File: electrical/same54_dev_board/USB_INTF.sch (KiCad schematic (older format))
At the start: 3 parts, among them J1 USB_B_Micro, U2 FT232RQ-REEL

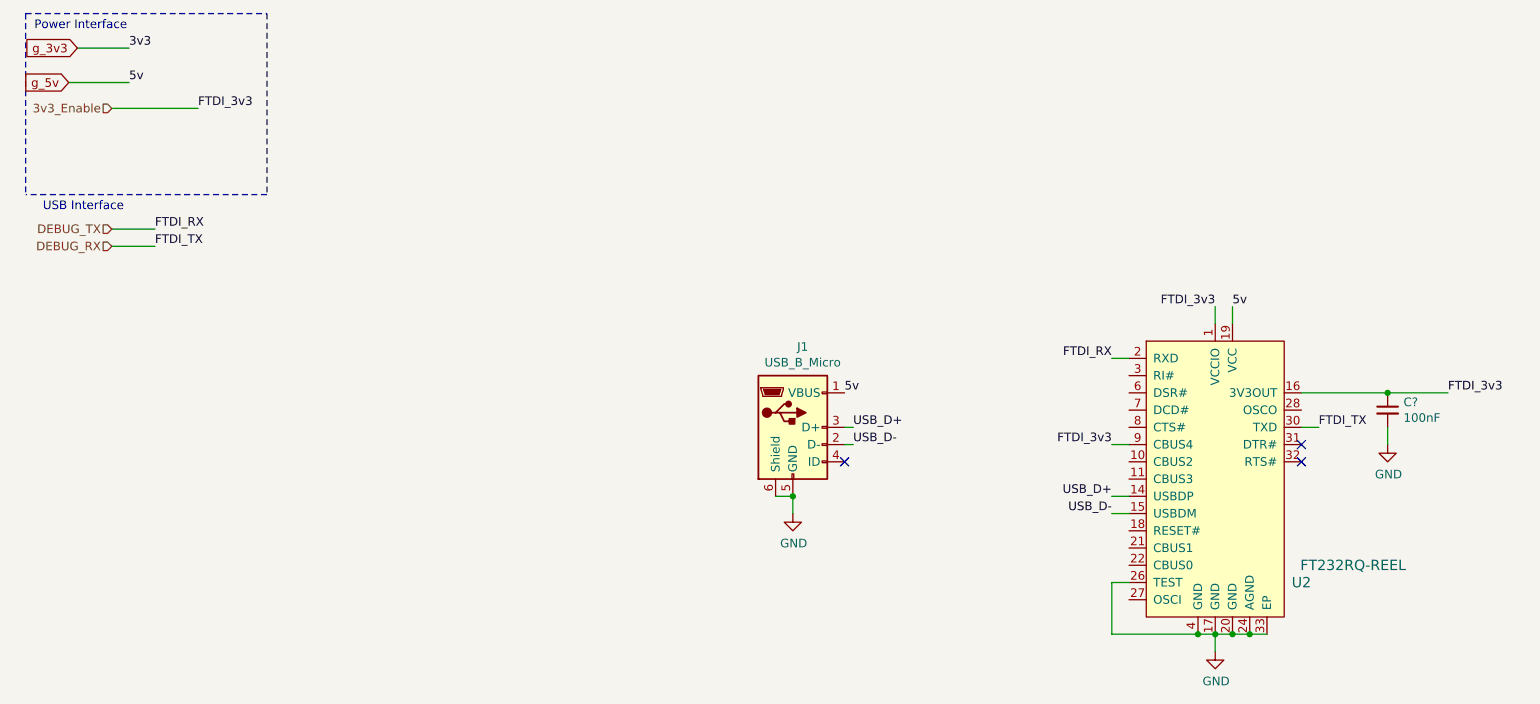
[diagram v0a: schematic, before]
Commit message: going with barrel jack 5v+2A optional input, with usb supplying 400mA + 100mA for internals
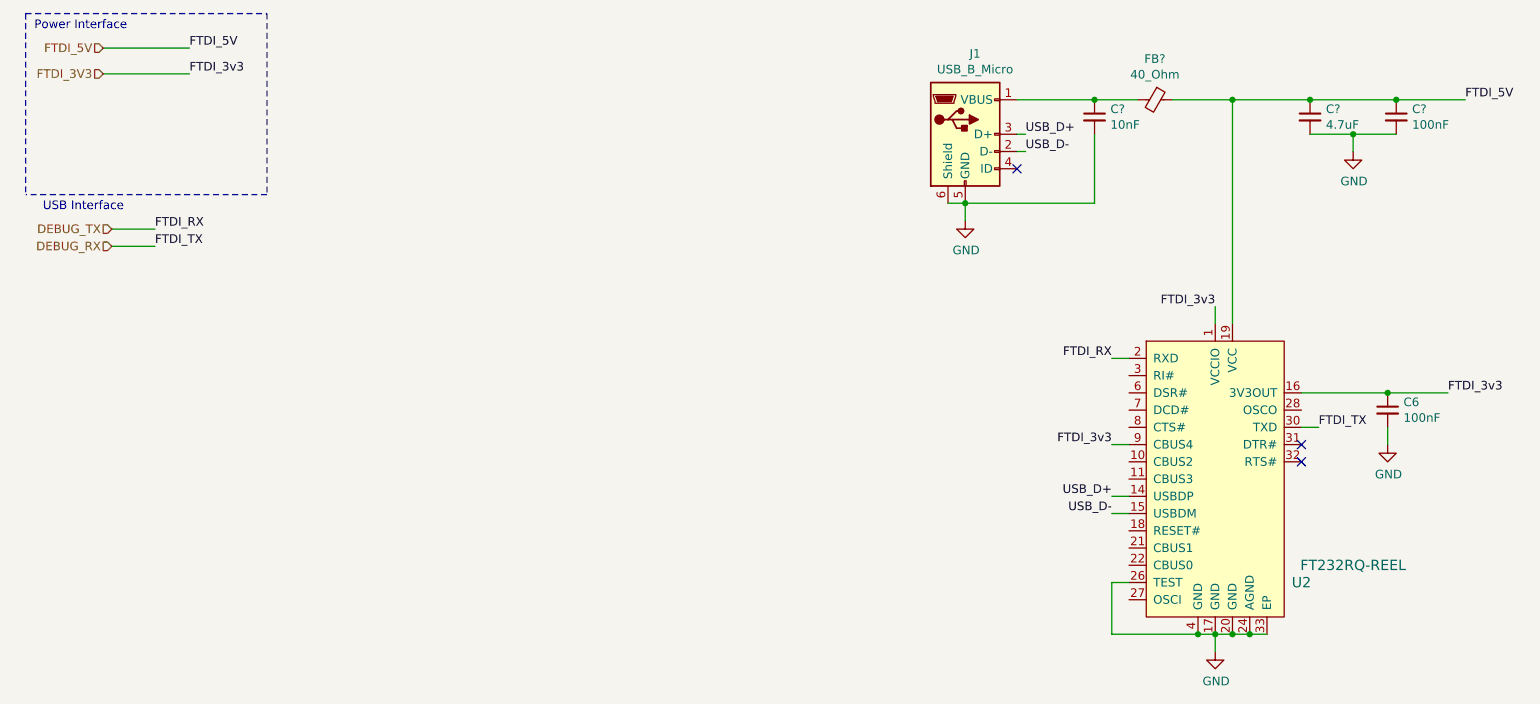
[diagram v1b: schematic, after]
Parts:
- added C?: 10nF, symbol Device:C_Small
- added C?: 4.7uF, symbol Device:C_Small
- added C?: 100nF, symbol Device:C_Small
- added FB?: 40_Ohm, symbol Device:Ferrite_Bead_Small
- gave numbers to parts that had none: 1
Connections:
- net GND: now also C?.2, C?.2, C?.2
- net 3v3_Enable renamed FTDI_3V3
- net g_5v: no longer names the net of J1.1 (VBUS)
- net g_5v: now also C?.1, FB?.2; no longer U2.19 (VCC)
- new net FTDI_5V: C?.1, C?.1, FB?.1, U2.19 (VCC)
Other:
- moved on the sheet: J1
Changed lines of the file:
@@
 Comment4 ""
 $EndDescr
-Text GLabel 900  800  0    50   Input ~ 0
-g_3v3
-Text GLabel 850  1000 0    50   Input ~ 0
-g_5v
-Wire Wire Line
-	900  800  1200 800
-Text Label 1200 800  0    50   ~ 0
-3v3
-Wire Wire Line
-	850  1000 1200 1000
-Text Label 1200 1000 0    50   ~ 0
-5v
 $Comp
 L Connector:USB_B_Micro J1
 U 1 1 5E8480AD
-P 5050 3000
-F 0 "J1" H 5107 3467 50  0000 C CNN
-F 1 "USB_B_Micro" H 5107 3376 50  0000 C CNN
-F 2 "Connector_USB:USB_Micro-B_Wuerth_629105150521" H 5200 2950 50  0001 C CNN
-F 3 "~" H 5200 2950 50  0001 C CNN
-	1    5050 3000
+P 6050 1300
+F 0 "J1" H 6107 1767 50  0000 C CNN
+F 1 "USB_B_Micro" H 6107 1676 50  0000 C CNN
+F 2 "Connector_USB:USB_Micro-B_Wuerth_629105150521" H 6200 1250 50  0001 C CNN
+F 3 "~" H 6200 1250 50  0001 C CNN
+	1    6050 1300
 	1    0    0    -1
 $EndComp
@@
 Power Interface
 Wire Wire Line
-	5350 3000 5400 3000
-Text Label 5400 3000 0    50   ~ 0
+	6350 1300 6400 1300
+Text Label 6400 1300 0    50   ~ 0
 USB_D+
 Wire Wire Line
-	5350 3100 5400 3100
-Text Label 5400 3100 0    50   ~ 0
+	6350 1400 6400 1400
+Text Label 6400 1400 0    50   ~ 0
 USB_D-
 Wire Wire Line
@@
 	7500 4200 7500 4300
 $Comp
-L power:GND #PWR?
+L power:GND #PWR0110
 U 1 1 5E7B73F2
 P 7500 4300
-F 0 "#PWR?" H 7500 4050 50  0001 C CNN
+F 0 "#PWR0110" H 7500 4050 50  0001 C CNN
 F 1 "GND" H 7505 4127 50  0000 C CNN
 F 2 "" H 7500 4300 50  0001 C CNN
@@
 $EndComp
 Wire Wire Line
-	4950 3400 5050 3400
-Wire Wire Line
-	5050 3400 5050 3500
-Connection ~ 5050 3400
-$Comp
-L power:GND #PWR?
+	5950 1700 6050 1700
+Wire Wire Line
+	6050 1700 6050 1800
+Connection ~ 6050 1700
+$Comp
+L power:GND #PWR0111
 U 1 1 5E7BED3A
-P 5050 3500
-F 0 "#PWR?" H 5050 3250 50  0001 C CNN
-F 1 "GND" H 5055 3327 50  0000 C CNN
-F 2 "" H 5050 3500 50  0001 C CNN
-F 3 "" H 5050 3500 50  0001 C CNN
-	1    5050 3500
-	1    0    0    -1
-$EndComp
-Text Label 5350 2800 0    50   ~ 0
-5v
-NoConn ~ 5350 3200
+P 6050 1800
+F 0 "#PWR0111" H 6050 1550 50  0001 C CNN
+F 1 "GND" H 6055 1627 50  0000 C CNN
+F 2 "" H 6050 1800 50  0001 C CNN
+F 3 "" H 6050 1800 50  0001 C CNN
+	1    6050 1800
+	1    0    0    -1
+$EndComp
+NoConn ~ 6350 1500
 Wire Notes Line
 	600  600  2000 600
-Wire Wire Line
-	7600 2400 7600 2300
-Text Label 7600 2300 0    50   ~ 0
-5v
 Text Label 1350 1950 0    50   ~ 0
 FTDI_TX
@@
 Text Notes 700  1750 0    50   ~ 0
 USB Interface
-Text HLabel 1100 1150 0    50   Input ~ 0
-3v3_Enable
 Wire Notes Line
 	2000 1650 600  1650
 Wire Notes Line
-	2000 600  2000 1650
-Wire Notes Line
 	600  600  600  1650
 Wire Wire Line
 	7500 2300 7500 2400
 Wire Wire Line
-	1100 1150 1600 1150
-Text Label 1600 1150 0    50   ~ 0
-FTDI_3v3
-Wire Wire Line
 	8000 2800 8500 2800
 $Comp
-L Device:C_Small C?
+L Device:C_Small C6
 U 1 1 5E7E8395
 P 8500 2900
-F 0 "C?" H 8592 2946 50  0000 L CNN
+F 0 "C6" H 8592 2946 50  0000 L CNN
 F 1 "100nF" H 8592 2855 50  0000 L CNN
 F 2 "" H 8500 2900 50  0001 C CNN
@@
 	8500 3000 8500 3100
 $Comp
-L power:GND #PWR?
+L power:GND #PWR0112
 U 1 1 5E7E91F3
 P 8500 3100
-F 0 "#PWR?" H 8500 2850 50  0001 C CNN
+F 0 "#PWR0112" H 8500 2850 50  0001 C CNN
 F 1 "GND" H 8505 2927 50  0000 C CNN
 F 2 "" H 8500 3100 50  0001 C CNN
@@
 	7700 4200 7800 4200
 Connection ~ 7700 4200
+$Comp
+L Device:C_Small C?
+U 1 1 5E7F85B7
+P 6800 1200
+F 0 "C?" H 6892 1246 50  0000 L CNN
+F 1 "10nF" H 6892 1155 50  0000 L CNN
+F 2 "" H 6800 1200 50  0001 C CNN
+F 3 "~" H 6800 1200 50  0001 C CNN
+	1    6800 1200
+	1    0    0    -1
+$EndComp
+Wire Wire Line
+	6350 1100 6800 1100
+Wire Wire Line
+	6800 1300 6800 1700
+Wire Wire Line
+	6800 1700 6050 1700
+Wire Wire Line
+	6800 1100 7050 1100
+Connection ~ 6800 1100
+$Comp
+L Device:Ferrite_Bead_Small FB?
+U 1 1 5E7FB1E4
+P 7150 1100
+F 0 "FB?" V 6913 1100 50  0000 C CNN
+F 1 "40_Ohm" V 7004 1100 50  0000 C CNN
+F 2 "" V 7080 1100 50  0001 C CNN
+F 3 "~" H 7150 1100 50  0001 C CNN
+	1    7150 1100
+	0    1    1    0
+$EndComp
+Wire Wire Line
+	7600 1100 7600 2400
+Wire Wire Line
+	7250 1100 7600 1100
+Wire Wire Line
+	7600 1100 8050 1100
+Connection ~ 7600 1100
+$Comp
+L Device:C_Small C?
+U 1 1 5E8424CD
+P 8050 1200
+F 0 "C?" H 8142 1246 50  0000 L CNN
+F 1 "4.7uF" H 8142 1155 50  0000 L CNN
+F 2 "" H 8050 1200 50  0001 C CNN
+F 3 "~" H 8050 1200 50  0001 C CNN
+	1    8050 1200
+	1    0    0    -1
+$EndComp
+$Comp
+L Device:C_Small C?
+U 1 1 5E844B56
+P 8550 1200
+F 0 "C?" H 8642 1246 50  0000 L CNN
+F 1 "100nF" H 8642 1155 50  0000 L CNN
+F 2 "" H 8550 1200 50  0001 C CNN
+F 3 "~" H 8550 1200 50  0001 C CNN
+	1    8550 1200
+	1    0    0    -1
+$EndComp
+Wire Wire Line
+	8050 1100 8550 1100
+Connection ~ 8050 1100
+Wire Wire Line
+	8050 1300 8300 1300
+Wire Wire Line
+	8300 1300 8300 1400
+Connection ~ 8300 1300
+Wire Wire Line
+	8300 1300 8550 1300
+$Comp
+L power:GND #PWR?
+U 1 1 5E849ABD
+P 8300 1400
+F 0 "#PWR?" H 8300 1150 50  0001 C CNN
+F 1 "GND" H 8305 1227 50  0000 C CNN
+F 2 "" H 8300 1400 50  0001 C CNN
+F 3 "" H 8300 1400 50  0001 C CNN
+	1    8300 1400
+	1    0    0    -1
+$EndComp
+Text Label 8950 1100 0    50   ~ 0
+FTDI_5V
+Wire Wire Line
+	8550 1100 8950 1100
+Connection ~ 8550 1100
+Wire Wire Line
+	1050 800  1550 800
+Text Label 1550 800  0    50   ~ 0
+FTDI_5V
+Text HLabel 1050 800  0    50   Input ~ 0
+FTDI_5V
+Text Label 1550 950  0    50   ~ 0
+FTDI_3v3
+Wire Wire Line
+	1050 950  1550 950
+Wire Notes Line
+	2000 600  2000 1650
+Text HLabel 1050 950  0    50   Input ~ 0
+FTDI_3V3
 $EndSCHEMATC

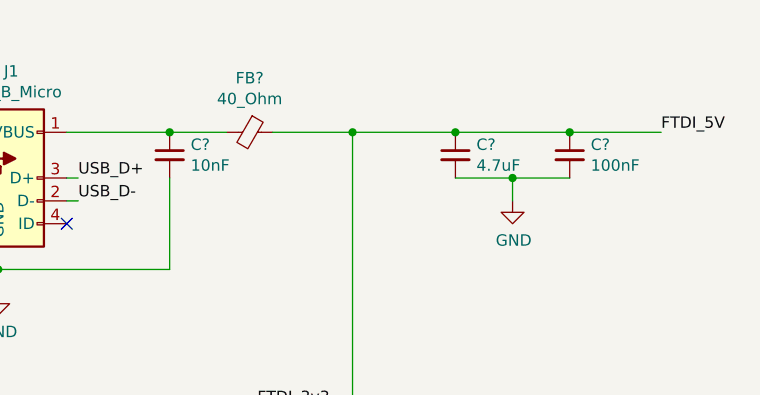
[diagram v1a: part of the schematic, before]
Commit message: Added usart, i2c, and spi pin locations, as well as labeled sercoms
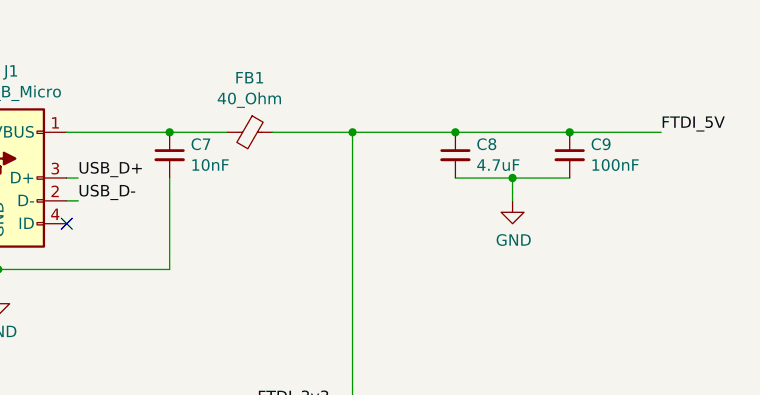
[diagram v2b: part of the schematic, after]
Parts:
- gave numbers to parts that had none: 4
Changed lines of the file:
@@
 Connection ~ 7700 4200
 $Comp
-L Device:C_Small C?
+L Device:C_Small C7
 U 1 1 5E7F85B7
 P 6800 1200
-F 0 "C?" H 6892 1246 50  0000 L CNN
+F 0 "C7" H 6892 1246 50  0000 L CNN
 F 1 "10nF" H 6892 1155 50  0000 L CNN
 F 2 "" H 6800 1200 50  0001 C CNN
@@
 Connection ~ 6800 1100
 $Comp
-L Device:Ferrite_Bead_Small FB?
+L Device:Ferrite_Bead_Small FB1
 U 1 1 5E7FB1E4
 P 7150 1100
-F 0 "FB?" V 6913 1100 50  0000 C CNN
+F 0 "FB1" V 6913 1100 50  0000 C CNN
 F 1 "40_Ohm" V 7004 1100 50  0000 C CNN
 F 2 "" V 7080 1100 50  0001 C CNN
@@
 Connection ~ 7600 1100
 $Comp
-L Device:C_Small C?
+L Device:C_Small C8
 U 1 1 5E8424CD
 P 8050 1200
-F 0 "C?" H 8142 1246 50  0000 L CNN
+F 0 "C8" H 8142 1246 50  0000 L CNN
 F 1 "4.7uF" H 8142 1155 50  0000 L CNN
 F 2 "" H 8050 1200 50  0001 C CNN
@@
 $EndComp
 $Comp
-L Device:C_Small C?
+L Device:C_Small C9
 U 1 1 5E844B56
 P 8550 1200
-F 0 "C?" H 8642 1246 50  0000 L CNN
+F 0 "C9" H 8642 1246 50  0000 L CNN
 F 1 "100nF" H 8642 1155 50  0000 L CNN
 F 2 "" H 8550 1200 50  0001 C CNN
@@
 	8300 1300 8550 1300
 $Comp
-L power:GND #PWR?
+L power:GND #PWR0116
 U 1 1 5E849ABD
 P 8300 1400
-F 0 "#PWR?" H 8300 1150 50  0001 C CNN
+F 0 "#PWR0116" H 8300 1150 50  0001 C CNN
 F 1 "GND" H 8305 1227 50  0000 C CNN
 F 2 "" H 8300 1400 50  0001 C CNN
